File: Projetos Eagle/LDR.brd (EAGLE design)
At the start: 39.8 x 21.5 mm, 11 parts, among them J1 CONECTOR, J2 CONECTOR, U1 TL494BD

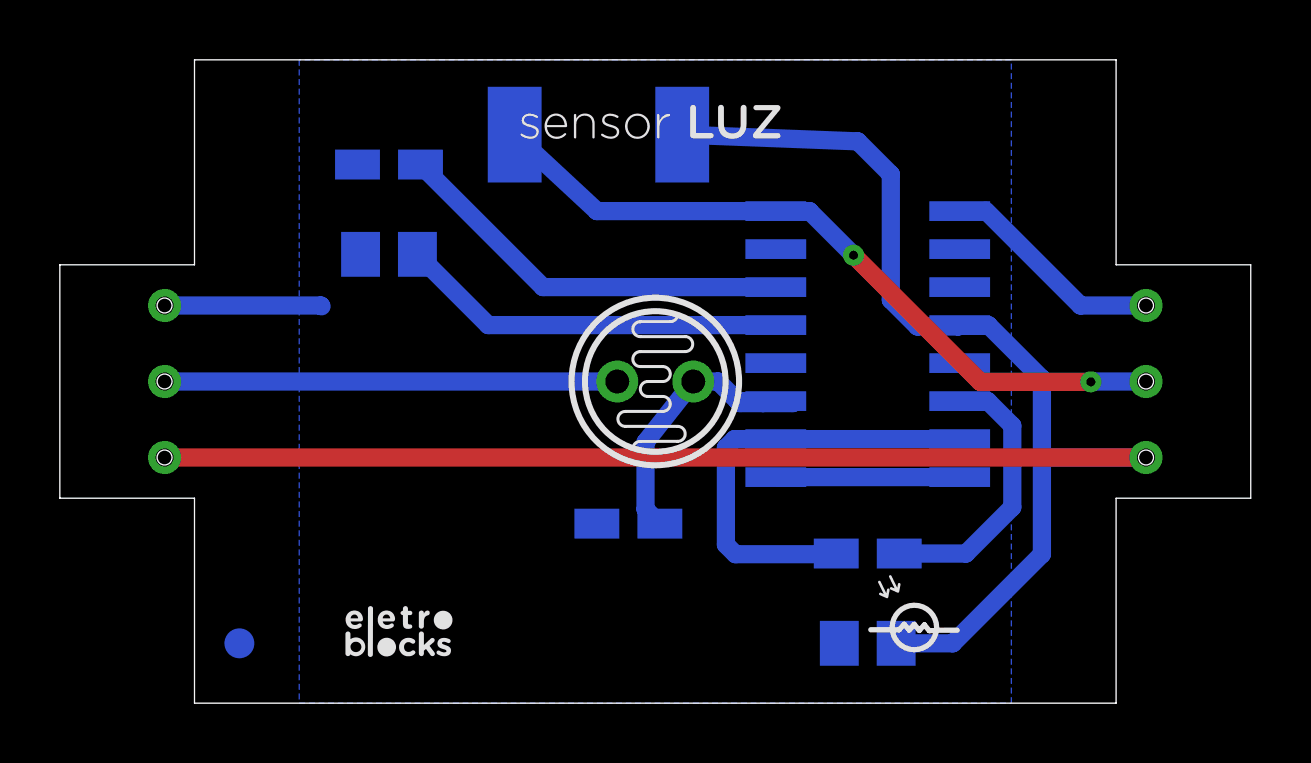
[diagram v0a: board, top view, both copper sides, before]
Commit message: correção de pads, adição de label para versionamento e plano de VCC
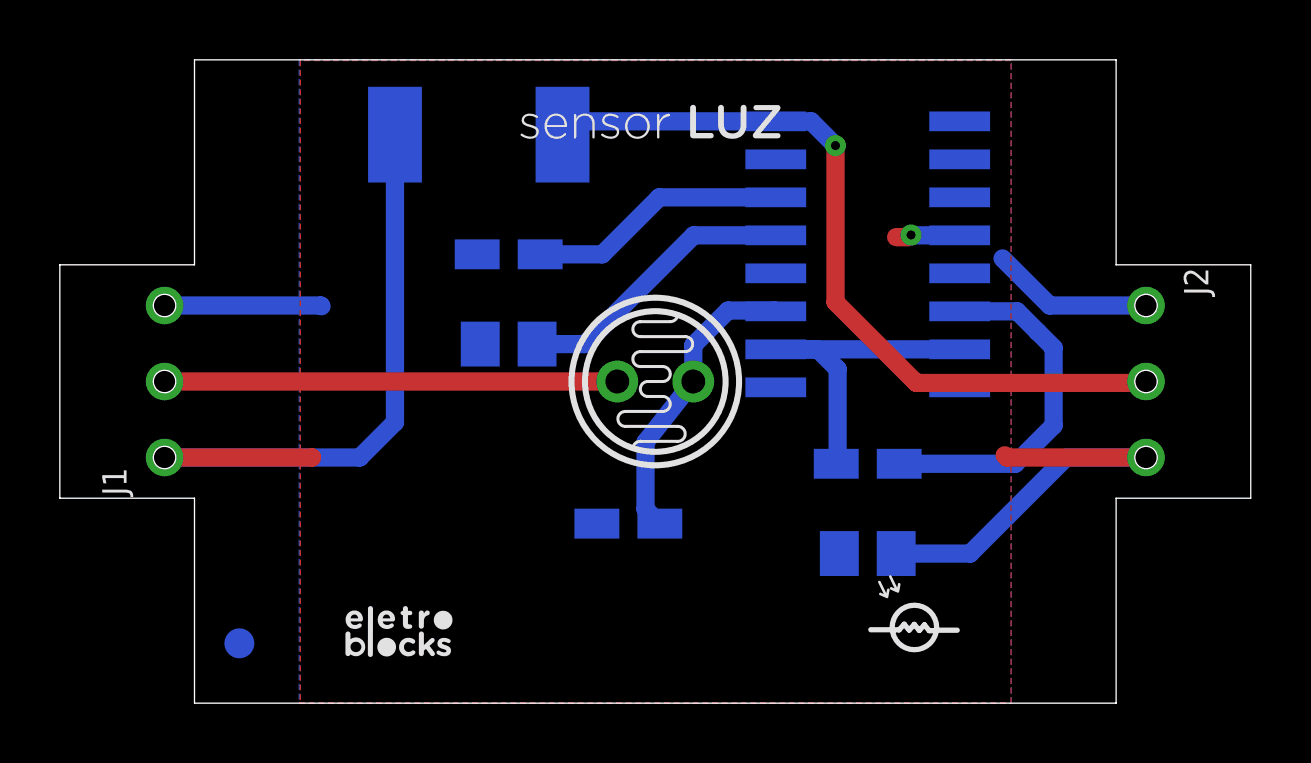
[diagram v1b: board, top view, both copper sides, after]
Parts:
- J1: value CONECTOR -> CONECTOR_MACHO
- J2: value CONECTOR -> CONECTOR_FEMEA
- R4: value 10K -> 1.6M
- moved C2 5.00 mm to (7.00, 12.0)
- moved R2 5.00 mm to (7.00, 15.0)
- moved R3 4.00 mm to (6.00, 19.0), turned to 0 degrees
- moved C1 3.00 mm to (19.0, 5.00)
- moved R1 3.00 mm to (19.0, 8.00)
- moved U1 3.00 mm to (19.0, 15.0)
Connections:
- removed net N$1: U1.1, U1.16
- net GND: now also U1.1, U1.16
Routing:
- net VCC: track 66.9 -> 39.3 mm, vias 0 -> 1
- net N$1: track 6.15 -> 0.00 mm
- net N$4: track 13.6 -> 8.66 mm
- net N$2: track 13.0 -> 9.48 mm
- net VREF: track 15.0 -> 11.7 mm
- net N$3: track 9.24 -> 11.9 mm
- net SIGNAL_OUT: track 24.5 -> 26.4 mm, vias 2 -> 1
- net LDR_SIGNAL: track 11.5 -> 9.96 mm
- net GND: track 12.1 -> 10.7 mm
- added copper zone on layer 1, net VCC
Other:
- board text added: "V1.0.1"

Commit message: adição de filtro no SIGNAL_OUT para correção do Duty Cycle
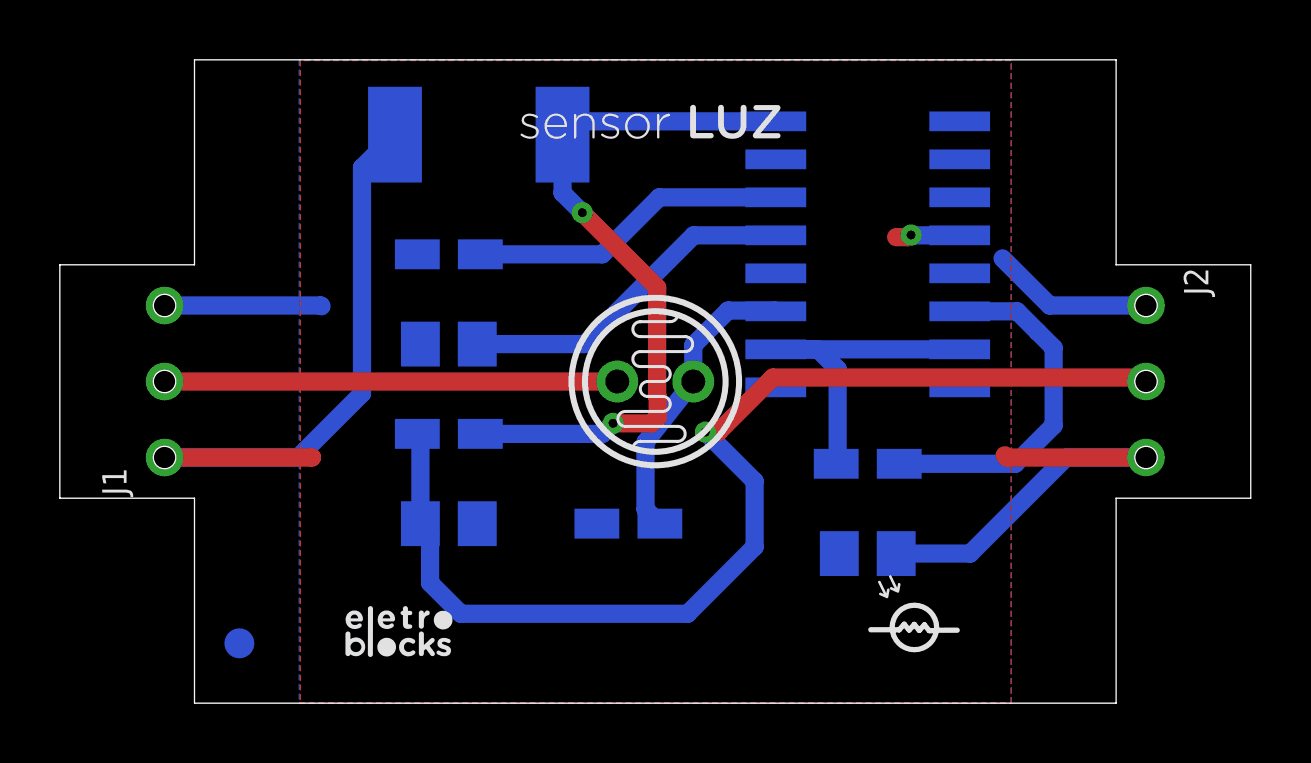
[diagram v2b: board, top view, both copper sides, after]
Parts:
- added C3: 100nF, rcl:C0805
- added R5: 1k, rcl:R0805W
- added U$2: (no value), Eletroblocks Lib:VERSAOATT
- moved C2 2.00 mm to (5.00, 12.0)
- moved R2 2.00 mm to (5.00, 15.0)
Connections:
- new net PWM: R3.1, R5.1, U1.8
- net GND: now also C3.1
- net SIGNAL_OUT: now also C3.2, R5.2; no longer R3.1, U1.8
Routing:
- net PWM: track 0.00 -> 24.2 mm, vias 0 -> 2
- net SIGNAL_OUT: track 26.4 -> 37.5 mm
- net N$4: track 8.66 -> 10.7 mm
- net N$2: track 9.48 -> 11.5 mm
- net VCC: track 39.3 -> 38.1 mm
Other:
- board text removed: "V1.0.1"

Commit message: correção de label
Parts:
- removed U$2: (no value), Eletroblocks Lib:VERSAOATT
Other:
- board text added: "V1.1.0"
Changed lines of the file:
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@@
 <drawing>
 <settings>
-<setting alwaysvectorfont="no"/>
+<setting alwaysvectorfont="yes"/>
 <setting verticaltext="up"/>
 </settings>
@@
 <vertex x="19.086075" y="2.36773125"/>
 </polygon>
+<text x="-0.3556" y="21.478240625" size="0.6096" layer="22" font="fixed" rot="MR270">V1.1.0</text>
 </plain>
 <attributes>
@@
 <attribute name="VALUE" x="6.27" y="3.46" size="1.27" layer="28" rot="MR0"/>
 </element>
-<element name="U$2" library="Eletroblocks Lib" package="VERSAOATT" value="" x="-0.604521875" y="21.3715625" smashed="yes" rot="R90"/>
 </elements>
 <signals>
